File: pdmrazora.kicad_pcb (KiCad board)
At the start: 2 copper layers, 150 x 130 mm, 53 parts, among them J1 9-6437287-8, J2 M6_VBAT_GND, M1000 Module:mega-mcu144/0.7, U1 BTS50010-1TAD, U11 BTS7004-1EPP, U12 BTS7004-1EPP, U13 BTS7004-1EPP, U14 BTS7004-1EPP, U15 BTS7004-1EPP, U16 BTS7004-1EPP, U17 BTS7004-1EPP, U18 BTS7004-1EPP, U2 BTS50010-1TAD, U3 BTS50010-1TAD, U4 BTS50010-1TAD

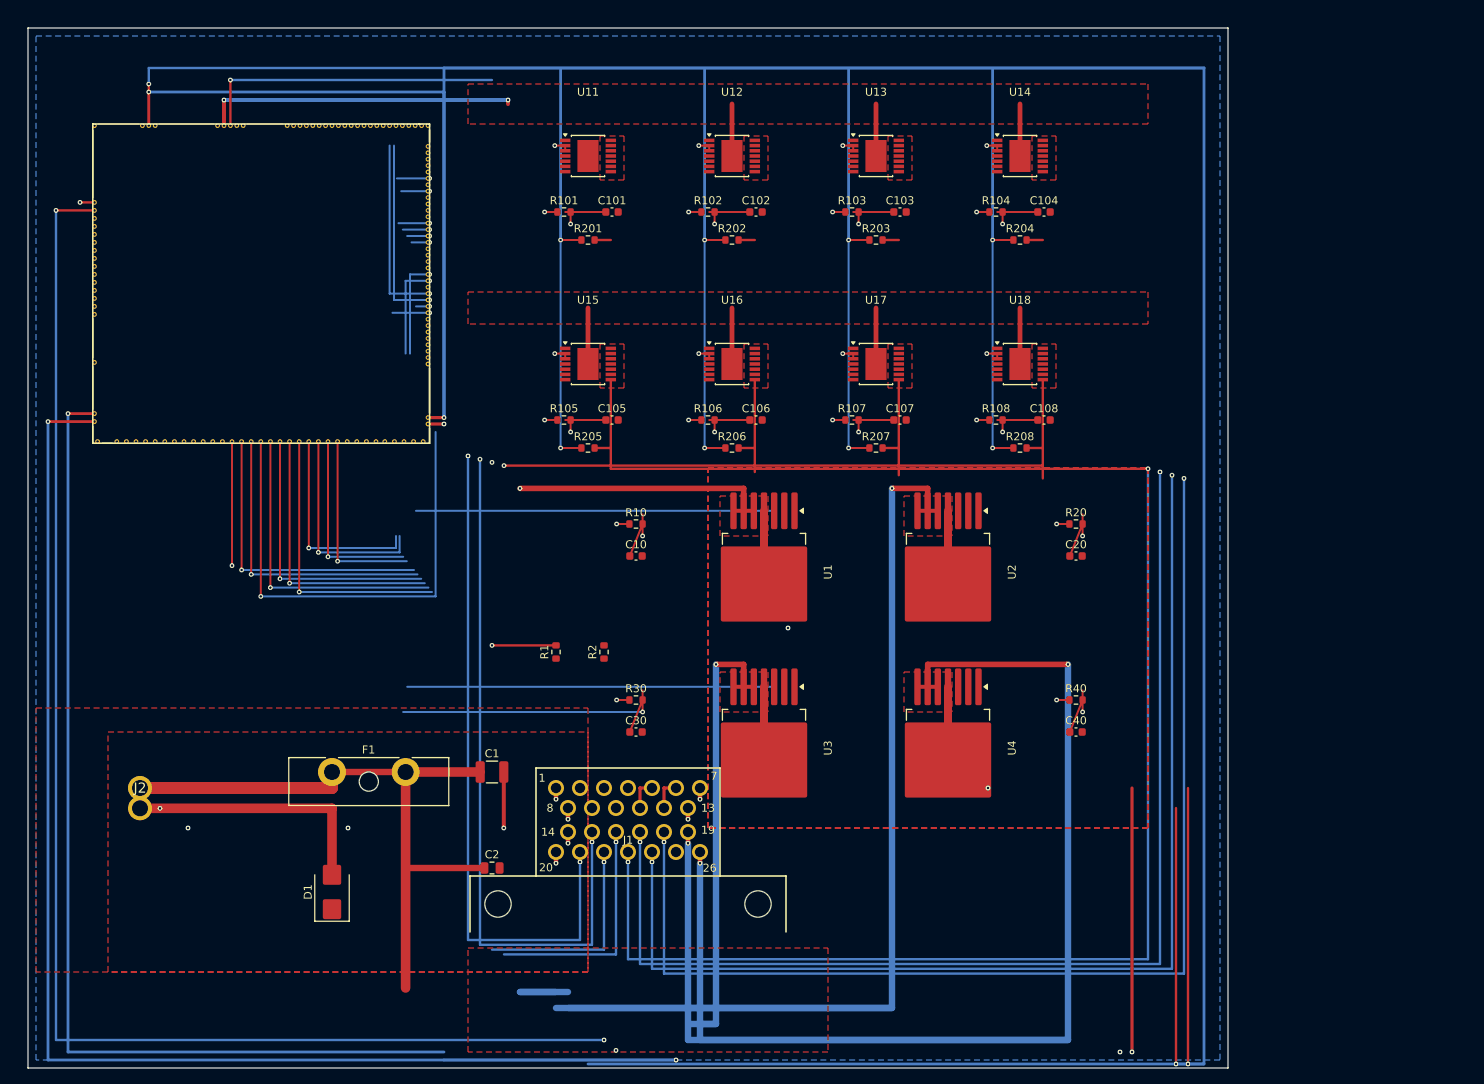
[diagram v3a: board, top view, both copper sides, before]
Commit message: Route EN exclusive B lanes; IS local + gated long-haul
After DRC cleanup 5f0f389: reconnect all 12 EN nets on exclusive B.Cu
corridors (HP south-ring, ADIO top/bot cols) and rebuild IS U–R–C local
sense without new shorts. Keep three IS long-haul nets (AUX1/AUX4/MAP1)
via per-net DRC gate; nine IS ratsnest remain. Unconnected 145→122;
shorts stay at J2-only; K8 headers preserved; HELLCORE untouched.
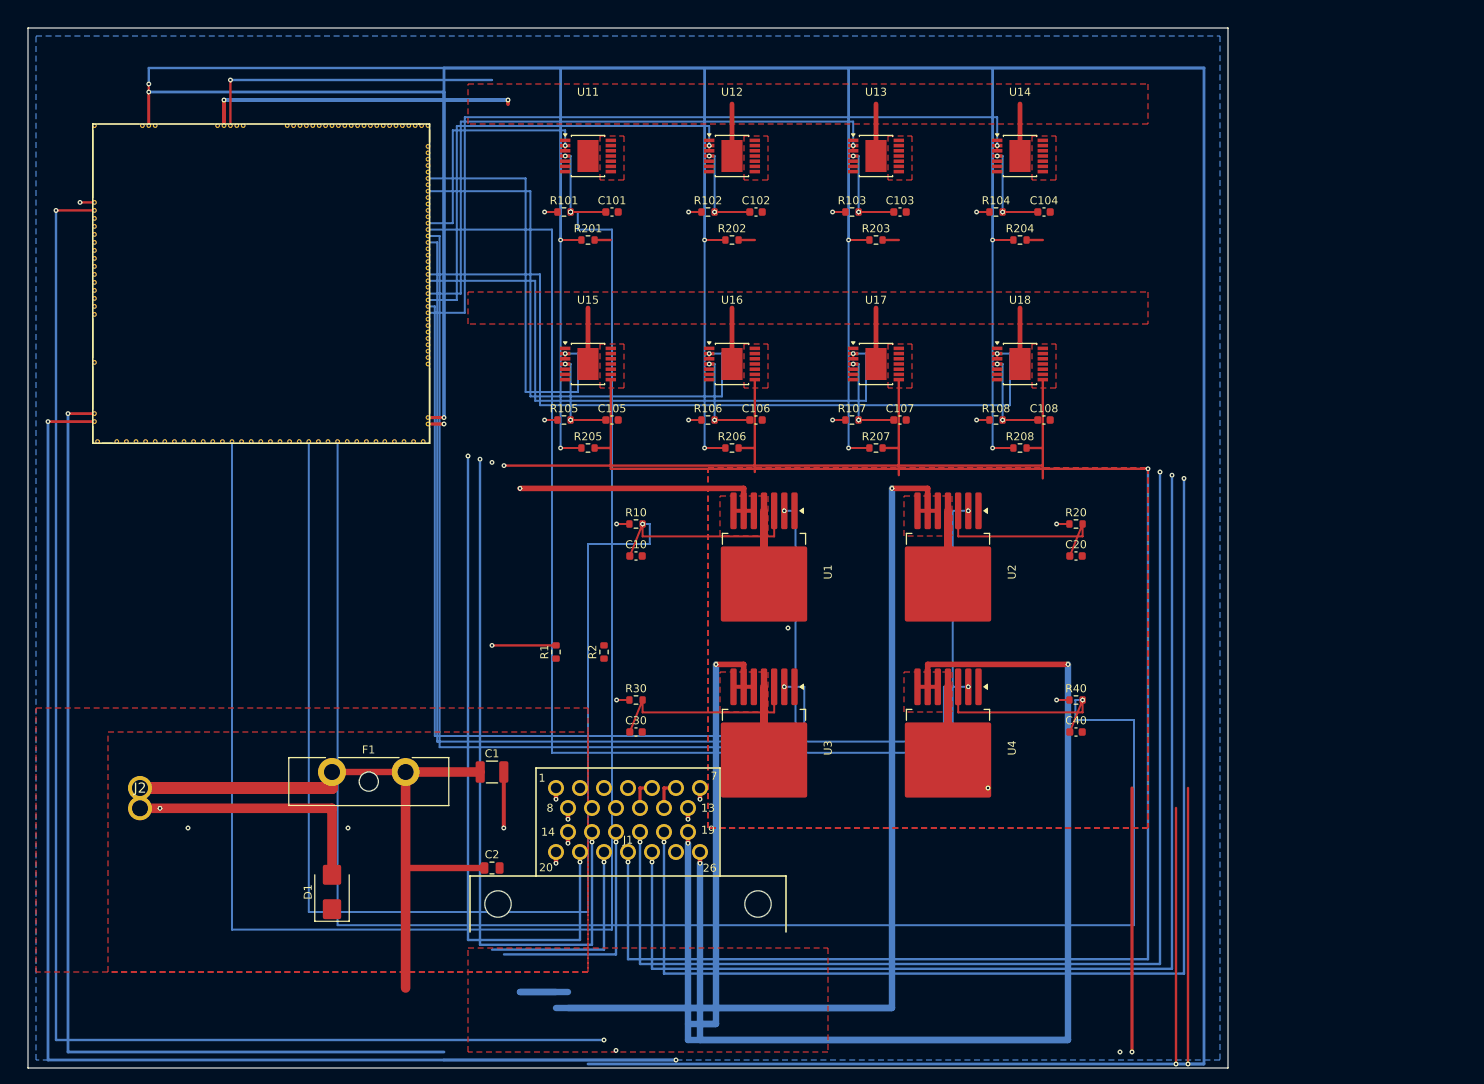
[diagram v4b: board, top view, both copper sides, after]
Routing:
- net IN_MAP1: track 22.1 -> 215.4 mm, vias 2 -> 3
- net IN_AUX4: track 31.1 -> 221.0 mm, vias 2 -> 1
- net OUT_PWM2: track 2.45 -> 158.8 mm
- net IN_AUX1: track 33.2 -> 176.3 mm, vias 2 -> 1
- net OUT_PWM4: track 3.55 -> 141.2 mm
- net OUT_PWM8: track 6.80 -> 99.8 mm, vias 2 -> 1
- net OUT_IO8: track 14.5 -> 97.8 mm, vias 2 -> 1
- net OUT_PWM1: track 46.6 -> 129.2 mm
- net OUT_PWM3: track 48.8 -> 121.0 mm
- net OUT_IO6: track 5.70 -> 70.0 mm, vias 2 -> 1
- net OUT_IO7: track 14.2 -> 77.9 mm, vias 2 -> 1
- net IN_RES3: track 68.3 -> 12.1 mm
- net OUT_PWM7: track 25.7 -> 78.3 mm, vias 2 -> 1
- net OUT_IO5: track 6.25 -> 52.5 mm, vias 2 -> 1
- net IN_AUX3: track 61.2 -> 25.5 mm, vias 2 -> 0
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
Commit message: Route remaining 9 IS long-haul nets and thin EN B lanes
Gated B.Cu south-ring closes AUX2/3, MAP2/3, O2S/O2S2, and RES1–3
without new shorts (J2 VBAT↔GND remains the only short). EN B
re-geometry stays north of PWR / south of SENSOR and keeps EN/IS
closed. Crossings rise 87→119 from IS highways vs ADIO/PWR; F
westbound + west-corridor cut is staged next. KiCad stem stays
pdmrazora; HELLCORE untouched; no PowerCore branding rename.

Co-authored-by: Quintin <quintinbannink42@users.noreply.github.com>
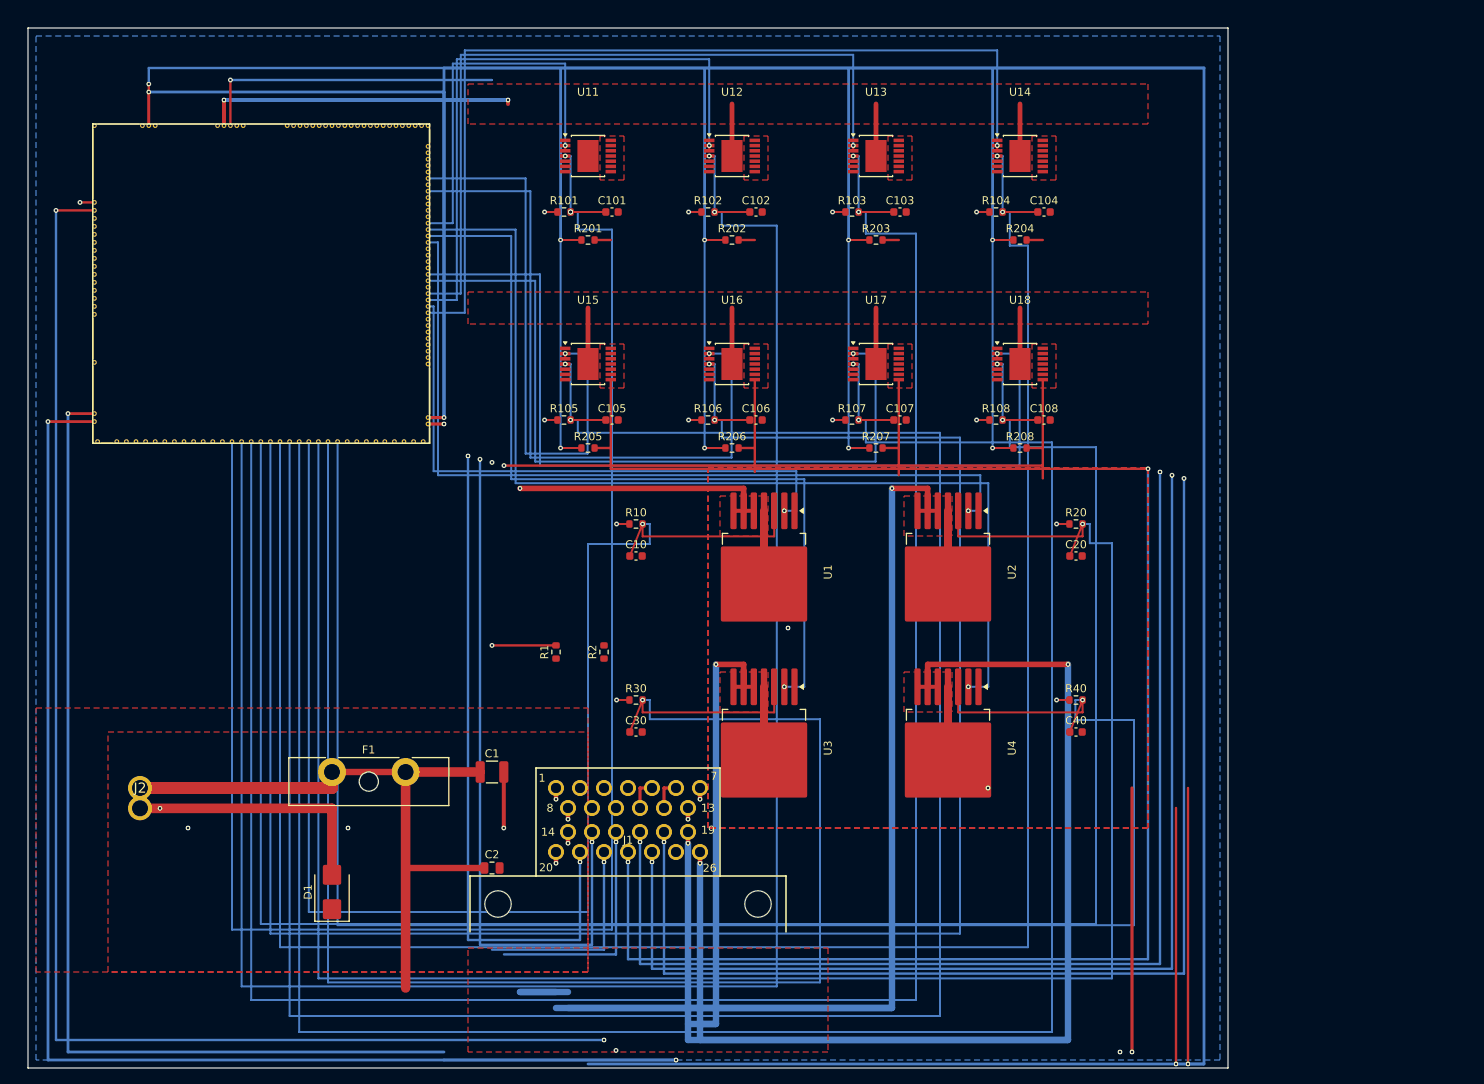
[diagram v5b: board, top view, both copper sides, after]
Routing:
- net IN_O2S2: track 12.1 -> 285.8 mm
- net IN_RES2: track 12.1 -> 280.6 mm
- net IN_MAP3: track 12.1 -> 270.6 mm
- net IN_O2S: track 12.1 -> 263.8 mm
- net IN_RES1: track 12.1 -> 254.6 mm
- net IN_MAP2: track 12.1 -> 251.6 mm
- net IN_RES3: track 12.1 -> 251.4 mm
- net IN_AUX2: track 24.6 -> 251.4 mm, vias 0 -> 1
- net IN_AUX3: track 25.5 -> 212.1 mm, vias 0 -> 1
- net OUT_PWM1: track 129.2 -> 73.1 mm
- net OUT_PWM2: track 158.8 -> 104.1 mm
- net OUT_IO5: track 52.5 -> 70.3 mm
- net OUT_IO6: track 70.0 -> 87.7 mm
- net OUT_IO7: track 77.9 -> 95.5 mm
- net OUT_IO8: track 97.8 -> 115.3 mm
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
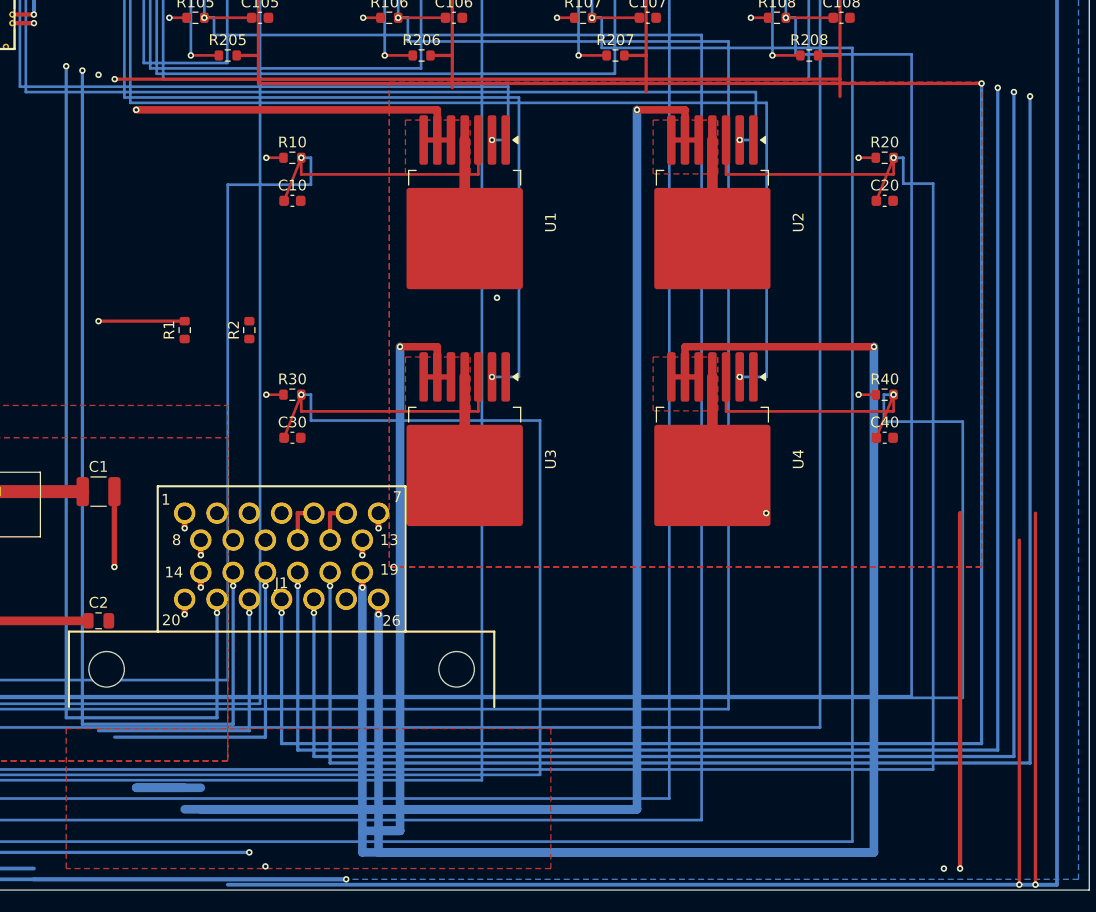
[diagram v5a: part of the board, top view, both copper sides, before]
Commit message: Trim ADIO J1 U-turns and drop orphan PWR south stubs
After the 9 IS long-haul fill (crossings 119), shift ADIO1–8 B.Cu U-turns
from y=114–118 to 105.4–106.9 so they sit north of the IS south-ring and
J1 mounting. Delete PWR_OUT B copper with y>110 that never reached the
J1 vias. Shorts stay J2-only; EN/IS stay closed. Crossings 87→106.
F westbound / via-hop / nested re-pair still short through F1/J1.
KiCad stem stays pdmrazora; no PowerCore branding; HELLCORE untouched.

Co-authored-by: Quintin <quintinbannink42@users.noreply.github.com>
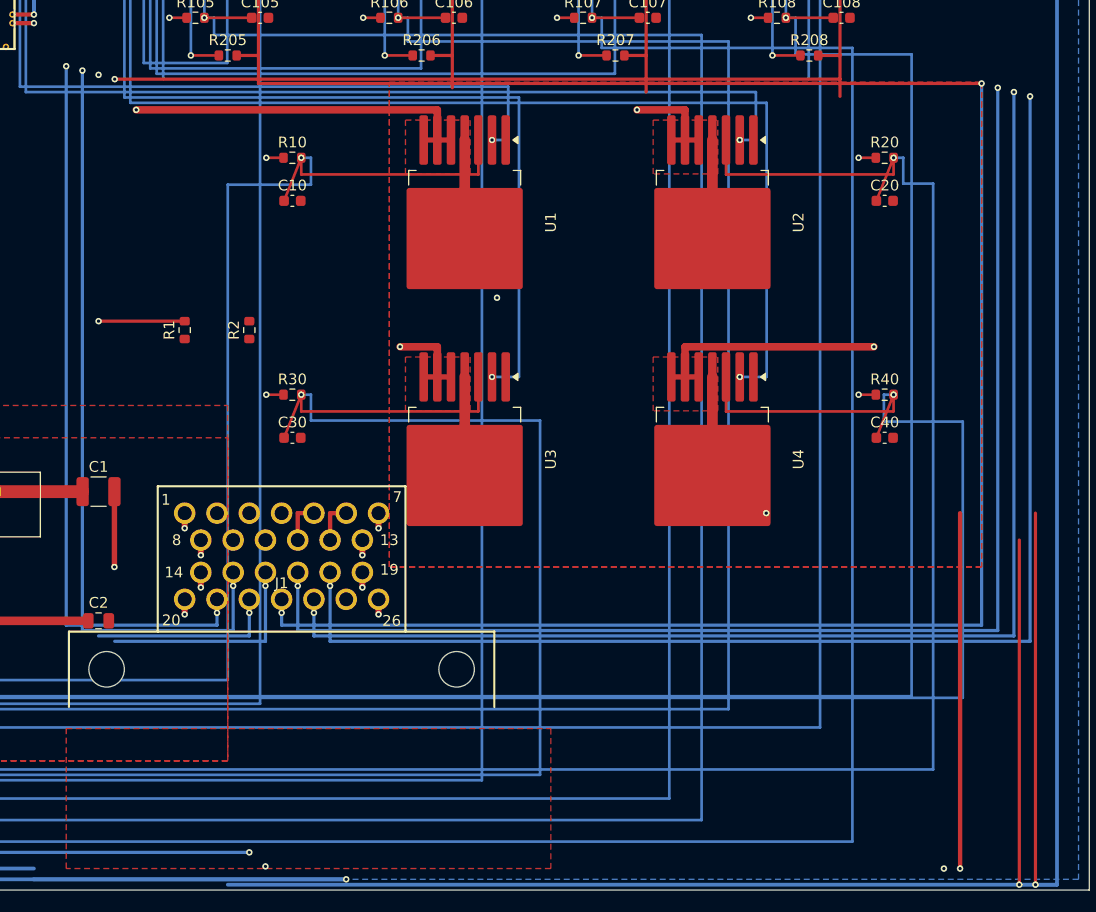
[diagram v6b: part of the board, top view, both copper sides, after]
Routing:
- net PWR_OUT4: track 212.8 -> 25.7 mm
- net PWR_OUT2: track 160.1 -> 12.6 mm
- net PWR_OUT3: track 62.1 -> 11.6 mm
- net ADIO8: track 159.0 -> 136.4 mm
- net ADIO7: track 155.3 -> 132.9 mm
- net ADIO6: track 156.6 -> 134.4 mm
- net ADIO5: track 220.0 -> 198.0 mm
- net ADIO2: track 90.8 -> 73.4 mm
- net ADIO1: track 87.5 -> 70.3 mm
- net PWR_OUT1: track 46.6 -> 36.1 mm
- net ADIO4: track 98.7 -> 89.8 mm
- net ADIO3: track 28.2 -> 19.4 mm
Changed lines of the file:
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@@
 		(aux_axis_origin 0 130)
 		(pcbplotparams
-			(layerselection 0x00000000_00000000_04821040_02b40309)
+			(layerselection 0x00000000_00000000_00931448_02140109)
 			(plot_on_all_layers_selection 0x00000000_00000000_00000000_00000000)
 			(disableapertmacros no)
@@
 	)
 	(segment
-		(start 61.5 120.5)
-		(end 67.5 120.5)
-		(width 0.8)
-		(layer "B.Cu")
-		(net 3)
-	)
-	(segment
-		(start 61.5 120.5)
-		(end 66 120.5)
-		(width 0.8)
-		(layer "B.Cu")
-		(net 3)
-	)
-	(segment
 		(start 112.46 57.55)
 		(end 108 57.55)
@@
 	)
 	(segment
-		(start 108 122.5)
-		(end 66 122.5)
-		(width 0.8)
-		(layer "B.Cu")
-		(net 4)
-	)
-	(segment
-		(start 108 57.55)
-		(end 108 122.5)
-		(width 0.8)
-		(layer "B.Cu")
-		(net 4)
-	)
-	(segment
-		(start 108 122.5)
-		(end 67.5 122.5)
-		(width 0.8)
-		(layer "B.Cu")
-		(net 4)
-	)
-	(segment
 		(start 89.46 79.55)
 		(end 86 79.55)
@@
 	)
 	(segment
-		(start 86 124.5)
-		(end 84 124.5)
-		(width 0.8)
-		(layer "B.Cu")
-		(net 5)
-	)
-	(segment
-		(start 86 79.55)
-		(end 86 124.5)
-		(width 0.8)
-		(layer "B.Cu")
-		(net 5)
-	)
-	(segment
-		(start 86 124.5)
-		(end 82.5 124.5)
-		(width 0.8)
-		(layer "B.Cu")
-		(net 5)
-	)
-	(segment
 		(start 82.5 101.9)
 		(end 82.5 100.5)
@@
 	)
 	(segment
-		(start 130 126.5)
-		(end 82.5 126.5)
-		(width 0.8)
-		(layer "B.Cu")
-		(net 6)
-	)
-	(segment
-		(start 130 79.55)
-		(end 130 126.5)
-		(width 0.8)
-		(layer "B.Cu")
-		(net 6)
-	)
-	(segment
-		(start 84 126.5)
-		(end 84 104.4)
-		(width 0.8)
-		(layer "B.Cu")
-		(net 6)
-	)
-	(segment
-		(start 130 126.5)
-		(end 84 126.5)
-		(width 0.8)
-		(layer "B.Cu")
-		(net 6)
-	)
-	(segment
-		(start 82.5 126.5)
-		(end 82.5 101.9)
-		(width 0.8)
-		(layer "B.Cu")
-		(net 6)
-	)
-	(segment
 		(start 8.299999 22.799996)
 		(end 3.5 22.799996)
@@
 	(segment
 		(start 55 53.5)
-		(end 55 114)
+		(end 55 105.4)
 		(width 0.3)
 		(layer "B.Cu")
@@
 	)
 	(segment
-		(start 55 114)
-		(end 69 114)
+		(start 55 105.4)
+		(end 69 105.4)
 		(width 0.3)
 		(layer "B.Cu")
@@
 	)
 	(segment
-		(start 69 114)
+		(start 69 105.4)
 		(end 69 104.25)
 		(width 0.3)
@@
 	)
 	(segment
-		(start 56.5 114.6)
-		(end 70.5 114.6)
+		(start 56.5 105.9)
+		(end 70.5 105.9)
 		(width 0.3)
 		(layer "B.Cu")
@@
 	(segment
 		(start 56.5 53.9)
-		(end 56.5 114.6)
+		(end 56.5 105.9)
 		(width 0.3)
 		(layer "B.Cu")
@@
 	)
 	(segment
-		(start 70.5 114.6)
+		(start 70.5 105.9)
 		(end 70.5 101.75)
 		(width 0.3)
@@
 	)
 	(segment
-		(start 58 115.2)
-		(end 72 115.2)
+		(start 58 106.4)
+		(end 72 106.4)
 		(width 0.3)
 		(layer "B.Cu")
@@
 	)
 	(segment
-		(start 72 115.2)
+		(start 72 106.4)
 		(end 72 104.25)
 		(width 0.3)
@@
 	)
 	(segment
-		(start 59.5 115.8)
-		(end 73.5 115.8)
+		(start 59.5 106.9)
+		(end 73.5 106.9)
 		(width 0.3)
 		(layer "B.Cu")
@@
 	)
 	(segment
-		(start 73.5 115.8)
+		(start 73.5 106.9)
 		(end 73.5 101.75)
 		(width 0.3)
@@
 	)
 	(segment
-		(start 75 116.4)
+		(start 75 105.4)
 		(end 75 104.25)
 		(width 0.3)
@@
 	)
 	(segment
-		(start 140 116.4)
-		(end 75 116.4)
+		(start 140 105.4)
+		(end 75 105.4)
 		(width 0.3)
 		(layer "B.Cu")
@@
 	(segment
 		(start 140 55.1)
-		(end 140 116.4)
+		(end 140 105.4)
 		(width 0.3)
 		(layer "B.Cu")
@@
 	)
 	(segment
-		(start 76.5 117)
+		(start 76.5 105.9)
 		(end 76.5 101.75)
 		(width 0.3)
@@
 	(segment
 		(start 141.5 55.5)
-		(end 141.5 117)
+		(end 141.5 105.9)
 		(width 0.3)
 		(layer "B.Cu")
@@
 	)
 	(segment
-		(start 141.5 117)
-		(end 76.5 117)
+		(start 141.5 105.9)
+		(end 76.5 105.9)
 		(width 0.3)
 		(layer "B.Cu")
@@
 	)
 	(segment
-		(start 78 117.6)
+		(start 78 106.4)
 		(end 78 104.25)
 		(width 0.3)
@@
 	(segment
 		(start 143 55.9)
-		(end 143 117.6)
+		(end 143 106.4)
 		(width 0.3)
 		(layer "B.Cu")
@@
 	)
 	(segment
-		(start 143 117.6)
-		(end 78 117.6)
+		(start 143 106.4)
+		(end 78 106.4)
 		(width 0.3)
 		(layer "B.Cu")
@@
 	)
 	(segment
-		(start 144.5 118.2)
-		(end 79.5 118.2)
+		(start 144.5 106.9)
+		(end 79.5 106.9)
 		(width 0.3)
 		(layer "B.Cu")
@@
 	)
 	(segment
-		(start 79.5 118.2)
+		(start 79.5 106.9)
 		(end 79.5 101.75)
 		(width 0.3)
@@
 	(segment
 		(start 144.5 56.3)
-		(end 144.5 118.2)
+		(end 144.5 106.9)
 		(width 0.3)
 		(layer "B.Cu")

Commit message: Cut DRC crossings 106→89 with gated EN/ADIO F-hops
Move AUX1 off J1 pins, F-hop EN over SENSOR x=52 and ADIO U-turns
across IS feeders. Shorts stay J2-only; EN/IS unconnected stay 0.

Co-authored-by: Quintin <quintinbannink42@users.noreply.github.com>
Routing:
- net IN_AUX1: track 176.3 -> 195.7 mm
- net IN_AUX4: track 221.0 -> 222.5 mm, vias 1 -> 3
- net OUT_PWM5: vias 1 -> 3
- net OUT_PWM4: vias 1 -> 3
- net OUT_IO5: vias 1 -> 3
- net OUT_PWM8: vias 1 -> 3
- net OUT_PWM7: vias 1 -> 3
- net OUT_PWM3: vias 1 -> 3
- net OUT_IO8: vias 1 -> 3
- net OUT_IO7: vias 1 -> 3
- net OUT_IO6: vias 1 -> 5
- net OUT_PWM6: vias 1 -> 3
- net IN_AUX2: vias 1 -> 3
- net ADIO8: vias 2 -> 4
- net ADIO7: vias 2 -> 4
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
